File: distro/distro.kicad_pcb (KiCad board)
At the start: 2 copper layers, 62.2 x 171.4 mm, 30 parts, among them K1 CONN_3, P1 CONN_2, P10 CONN_2, P11 CONN_2, P12 CONN_2, P2 CONN_2, P3 CONN_2, P4 CONN_2, P5 CONN_2, P6 CONN_2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

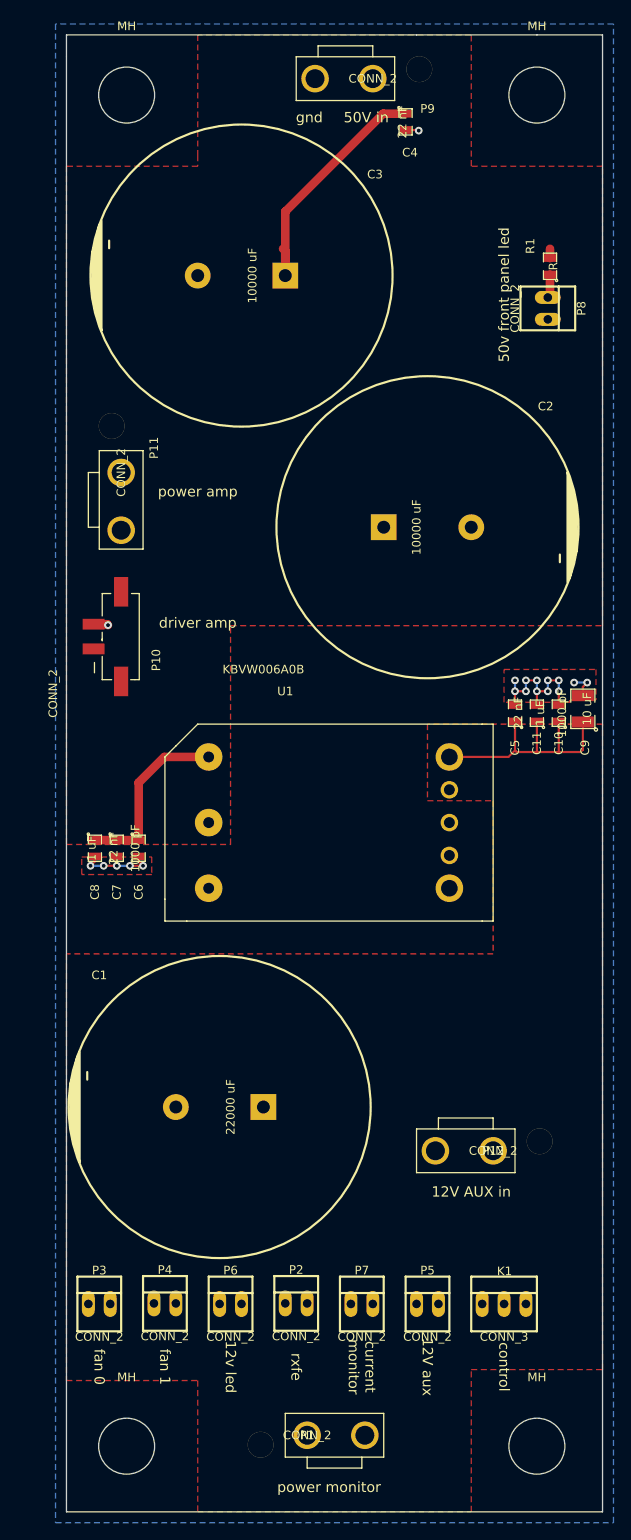
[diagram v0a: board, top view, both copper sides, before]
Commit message: started on t/r with enclosure, migrated distro to 15v
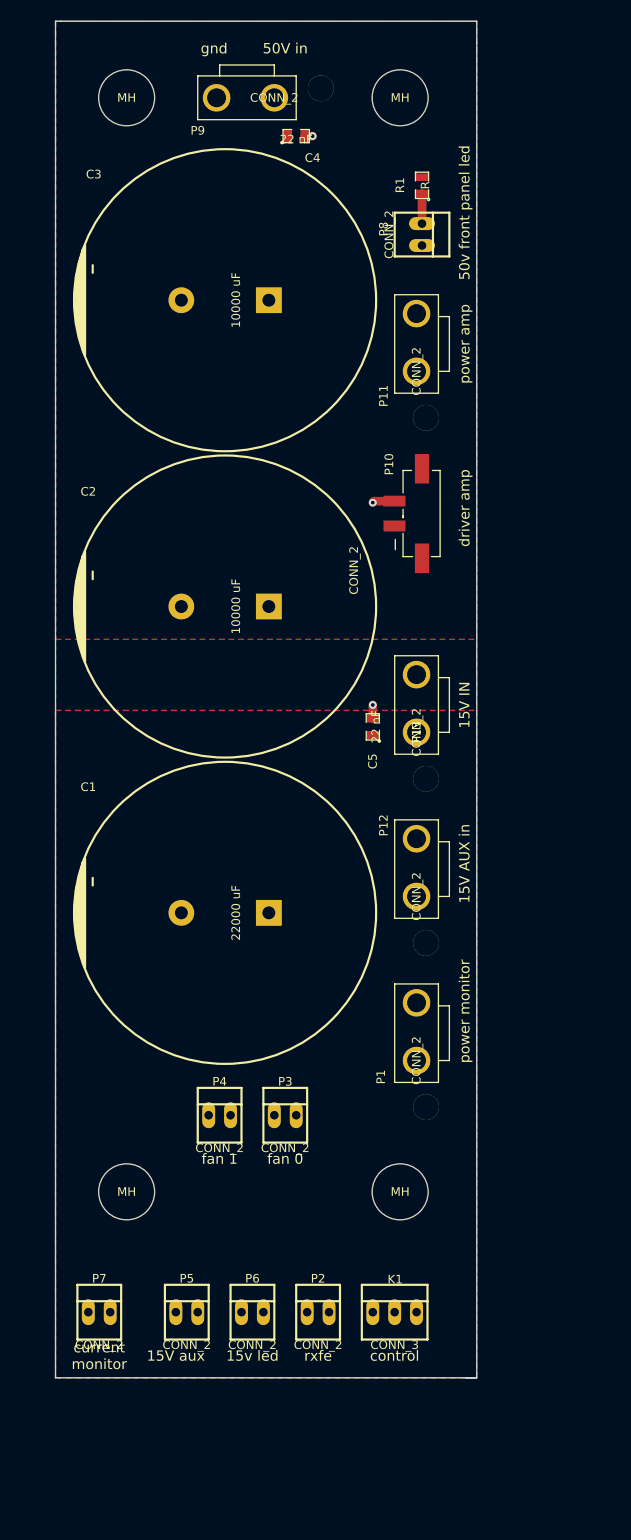
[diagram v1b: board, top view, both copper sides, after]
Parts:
- removed C10, C6: 1000 pF, SMD_Packages:SMD-0805
- removed C11, C8: 1 uF, SMD_Packages:SMD-0805
- removed C7: 22 nF, SMD_Packages:SMD-0805
- removed C9: 10 uF, SMD_Packages:SMD-1210
- removed the MH at (133.3, 179.1)
- removed the MH at (85.7, 179.1)
- removed the MH at (133.3, 22.2)
- removed the MH at (85.7, 22.2)
- removed U1: KBVW006A0B, local:KBVW006A0B
- added MH: MountingHole_6-5mm_RevA_Date21Jun2010, Mounting_Holes:MountingHole_6-5mm, F.Cu at (85.7, 22.5)
- added MH: MountingHole_6-5mm_RevA_Date21Jun2010, Mounting_Holes:MountingHole_6-5mm, F.Cu at (117.5, 22.5)
- added MH: MountingHole_6-5mm_RevA_Date21Jun2010, Mounting_Holes:MountingHole_6-5mm, F.Cu at (85.7, 149.5)
- added MH: MountingHole_6-5mm_RevA_Date21Jun2010, Mounting_Holes:MountingHole_6-5mm, F.Cu at (117.5, 149.5)
- added P13: CONN_2, local:0015311026, F.Cu at (119.4, 96.2)
- moved P1 45.3 mm to (119.4, 134.3), turned to 270 degrees
- moved P10 37.7 mm to (120.0, 70.8)
- moved P11 36.2 mm to (119.4, 54.3), turned to 270 degrees
- moved P12 30.8 mm to (119.4, 115.3), turned to 270 degrees
- moved P3 30.8 mm to (104.1, 140.7)
- moved P7 30.5 mm to (82.5, 163.5)
- moved P5 28.0 mm to (92.7, 163.5)
- moved C2 25.2 mm to (97.2, 81.6), turned to 90 degrees
- moved P4 22.7 mm to (96.5, 140.7)
- moved C1 22.6 mm to (97.2, 117.2)
- moved R1 17.6 mm to (120.0, 32.7)
- moved P8 16.9 mm to (120.0, 38.4)
- moved C5 16.6 mm to (114.3, 95.6)
- moved C4 12.8 mm to (105.4, 27.0), turned to 0 degrees
- moved K1 12.7 mm to (116.8, 163.5)
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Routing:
- net VCC: track 51.5 -> 0.00 mm
- net +12V: track 29.7 -> 0.00 mm
- net GND: track 32.5 -> 5.12 mm, vias 19 -> 3
- net Net-(P8-Pad1): track 2.77 -> 3.49 mm
- removed copper zone on F.Cu, net GND
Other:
- board size 62.2 x 171.4 mm -> 48.9 x 157.5 mm
- board text added: "15V AUX in"
- board text added: "15V IN"
- board text added: "15V aux"
- board text added: "15v led"
- board text added: "kodiak power distro 2014.09"
- board text removed: "12V AUX in"
- board text removed: "12V aux"
- board text removed: "12v led"

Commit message: component footprint changes to simplify bom
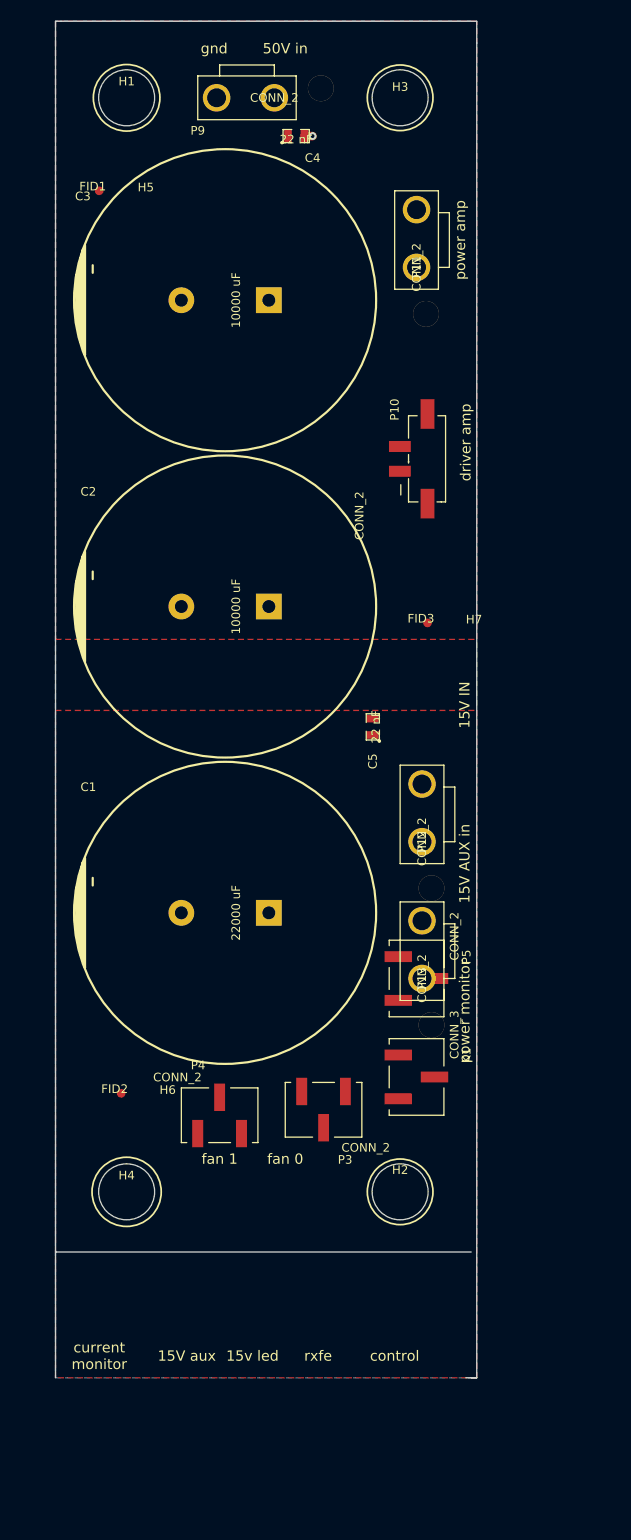
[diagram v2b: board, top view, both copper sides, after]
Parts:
- removed MH (x4): MountingHole_6-5mm_RevA_Date21Jun2010, Mounting_Holes:MountingHole_6-5mm
- removed P1: CONN_2, local:0015311026
- removed P2, P6, P7, P8: CONN_2, Connect:PINHEAD1-2
- removed R1: R, SMD_Packages:SMD-0805
- added H1: MOUNTING_HOLE, Mounting_Holes:MountingHole_6-5mm, F.Cu at (85.7, 22.5)
- added H2: MOUNTING_HOLE, Mounting_Holes:MountingHole_6-5mm, F.Cu at (117.5, 149.5)
- added H3: MOUNTING_HOLE, Mounting_Holes:MountingHole_6-5mm, F.Cu at (117.5, 22.5)
- added H4: MOUNTING_HOLE, Mounting_Holes:MountingHole_6-5mm, F.Cu at (85.7, 149.5)
- added H5: FID1, sdtransmitter:FID_1MM, F.Cu at (82.5, 33.3)
- added H6: FID2, sdtransmitter:FID_1MM, F.Cu at (85.1, 138.1)
- added H7: FID3, sdtransmitter:FID_1MM, F.Cu at (120.7, 83.5)
- K1: footprint Connect:PINHEAD1-3 -> sdtransmitter:0740991003
- P3, P4, P5: footprint Connect:PINHEAD1-2 -> sdtransmitter:0740991003
- moved P5 47.0 mm to (119.4, 124.8), turned to 270 degrees
- moved P13 28.6 mm to (120.0, 124.8)
- moved K1 27.4 mm to (119.4, 136.2), turned to 270 degrees
- moved P11 12.1 mm to (119.4, 42.2)
- moved P10 6.38 mm to (120.7, 64.5)
- moved P12 6.38 mm to (120.0, 108.9)
- moved P3 4.49 mm to (108.6, 140.0), turned to 180 degrees
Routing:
- net GND: track 5.12 -> 0.95 mm, vias 3 -> 1
- net Net-(P8-Pad1): track 3.49 -> 0.00 mm
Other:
- outline, holes or cut-outs redrawn
- board text removed: "50v front panel led"

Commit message: shrank power distro board for mounting on plate, updated transmitter plate drawings
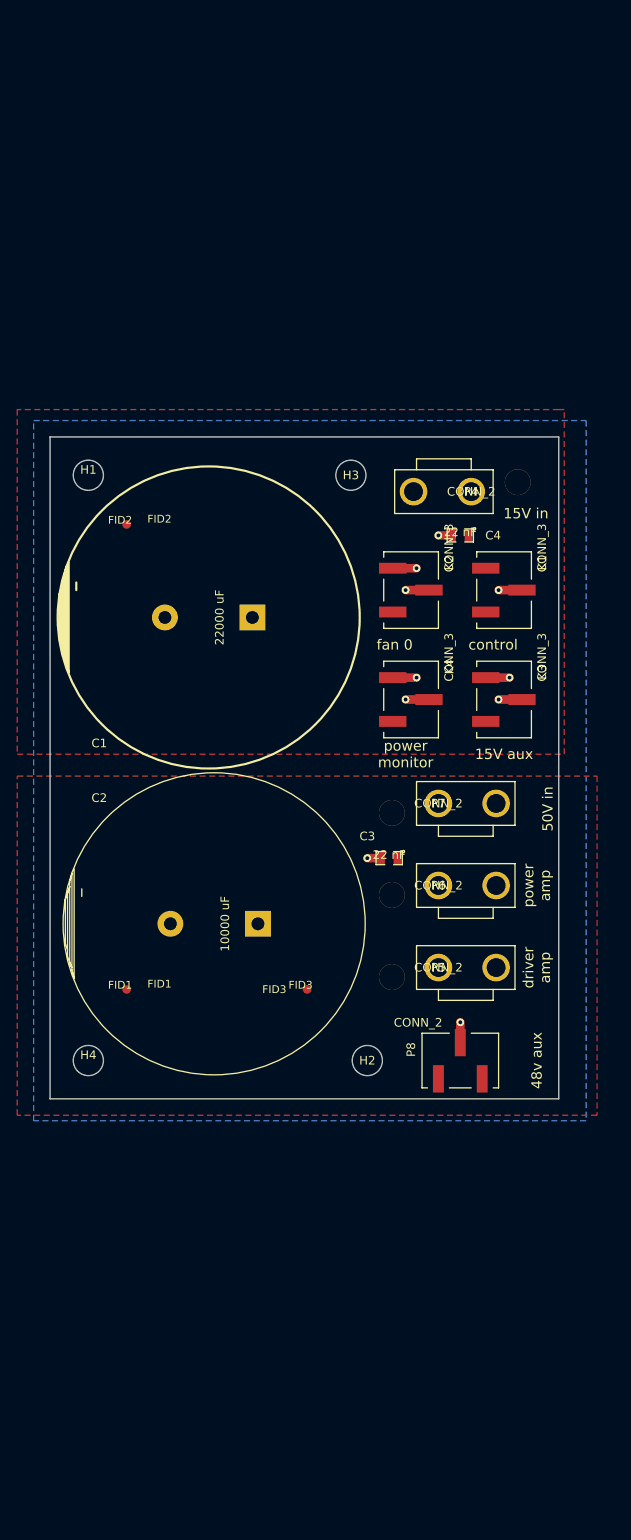
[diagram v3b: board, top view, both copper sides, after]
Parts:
- removed C5: 22 nF, SMD_Packages:SMD-0805
- removed H5: FID1, sdtransmitter:FID_1MM
- removed H6: FID2, sdtransmitter:FID_1MM
- removed H7: FID3, sdtransmitter:FID_1MM
- removed P10: CONN_2, local:2-1445053-2
- removed P11, P12, P13, P9: CONN_2, local:0015311026
- removed P3: CONN_2, sdtransmitter:0740991003
- added FID1: FID1, sdtransmitter:FID_1MM, F.Cu at (85.7, 126.0)
- added FID2: FID2, sdtransmitter:FID_1MM, F.Cu at (85.7, 72.1)
- added FID3: FID3, sdtransmitter:FID_1MM, F.Cu at (106.7, 126.0)
- added K2: CONN_3, sdtransmitter:0740991003, F.Cu at (118.7, 79.7)
- added K3: CONN_3, sdtransmitter:0740991003, F.Cu at (129.5, 92.4)
- added K4: CONN_3, sdtransmitter:0740991003, F.Cu at (118.7, 92.4)
- added P6: CONN_2, local:0015311026, F.Cu at (121.9, 114.0)
- added P7: CONN_2, local:0015311026, F.Cu at (121.9, 104.5)
- added P8: CONN_2, sdtransmitter:0740991003, F.Cu at (124.5, 134.3)
- C3: value 10000 uF -> 22 nF; footprint Capacitors_ThroughHole:Capacitor35x51RM10 -> SMD_Packages:SMD-0805
- H1, H2, H3, H4: footprint Mounting_Holes:MountingHole_6-5mm -> Mounting_Holes:MountingHole_3-5mm
- P4, P5: footprint sdtransmitter:0740991003 -> local:0015311026
- moved P4 78.1 mm to (125.7, 68.3)
- moved C3 67.5 mm to (116.2, 110.8), turned to 180 degrees
- moved K1 57.4 mm to (129.5, 79.7)
- moved C4 50.1 mm to (124.5, 73.3), turned to 180 degrees
- moved H3 44.2 mm to (111.8, 66.4)
- moved H1 44.0 mm to (81.3, 66.4)
- moved C2 36.9 mm to (95.9, 118.4)
- moved C1 34.3 mm to (95.2, 82.9)
- moved H4 15.9 mm to (81.3, 134.3)
- moved H2 15.7 mm to (113.7, 134.3)
- moved P5 2.84 mm to (121.9, 123.5), turned to 180 degrees
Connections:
- C4 pad 1: VCC -> +12V
- P4 pad 1: +12V -> GND
- P4 pad 2: GND -> +12V
- P5 pad 1: +12V -> GND
- P5 pad 2: GND -> VCC
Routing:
- net GND: track 0.95 -> 24.7 mm, vias 1 -> 10
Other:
- board size 48.9 x 157.5 mm -> 59.1 x 76.8 mm
- board text added: "15V in"
- board text added: "48v aux"
- board text added: "kodiak power distro 2015"
- board text removed: "15V AUX in"
- board text removed: "15V IN"
- board text removed: "15v led"
- board text removed: "current monitor"
- board text removed: "fan 1"
- board text removed: "gnd"
- board text removed: "kodiak power distro 2014.09"
- board text removed: "rxfe"
